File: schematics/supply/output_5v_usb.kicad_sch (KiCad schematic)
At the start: 79 parts, among them J2 USB_A, Q3 40N06, U10 LM2904, U11 IP2163, U12 LM2904, U13 TL432DBZ, U14 LM2904, U15 AMS1117-3.3, U2 EL817, U6 INA3221, U8 MC34063AD, U9 IRS2153S

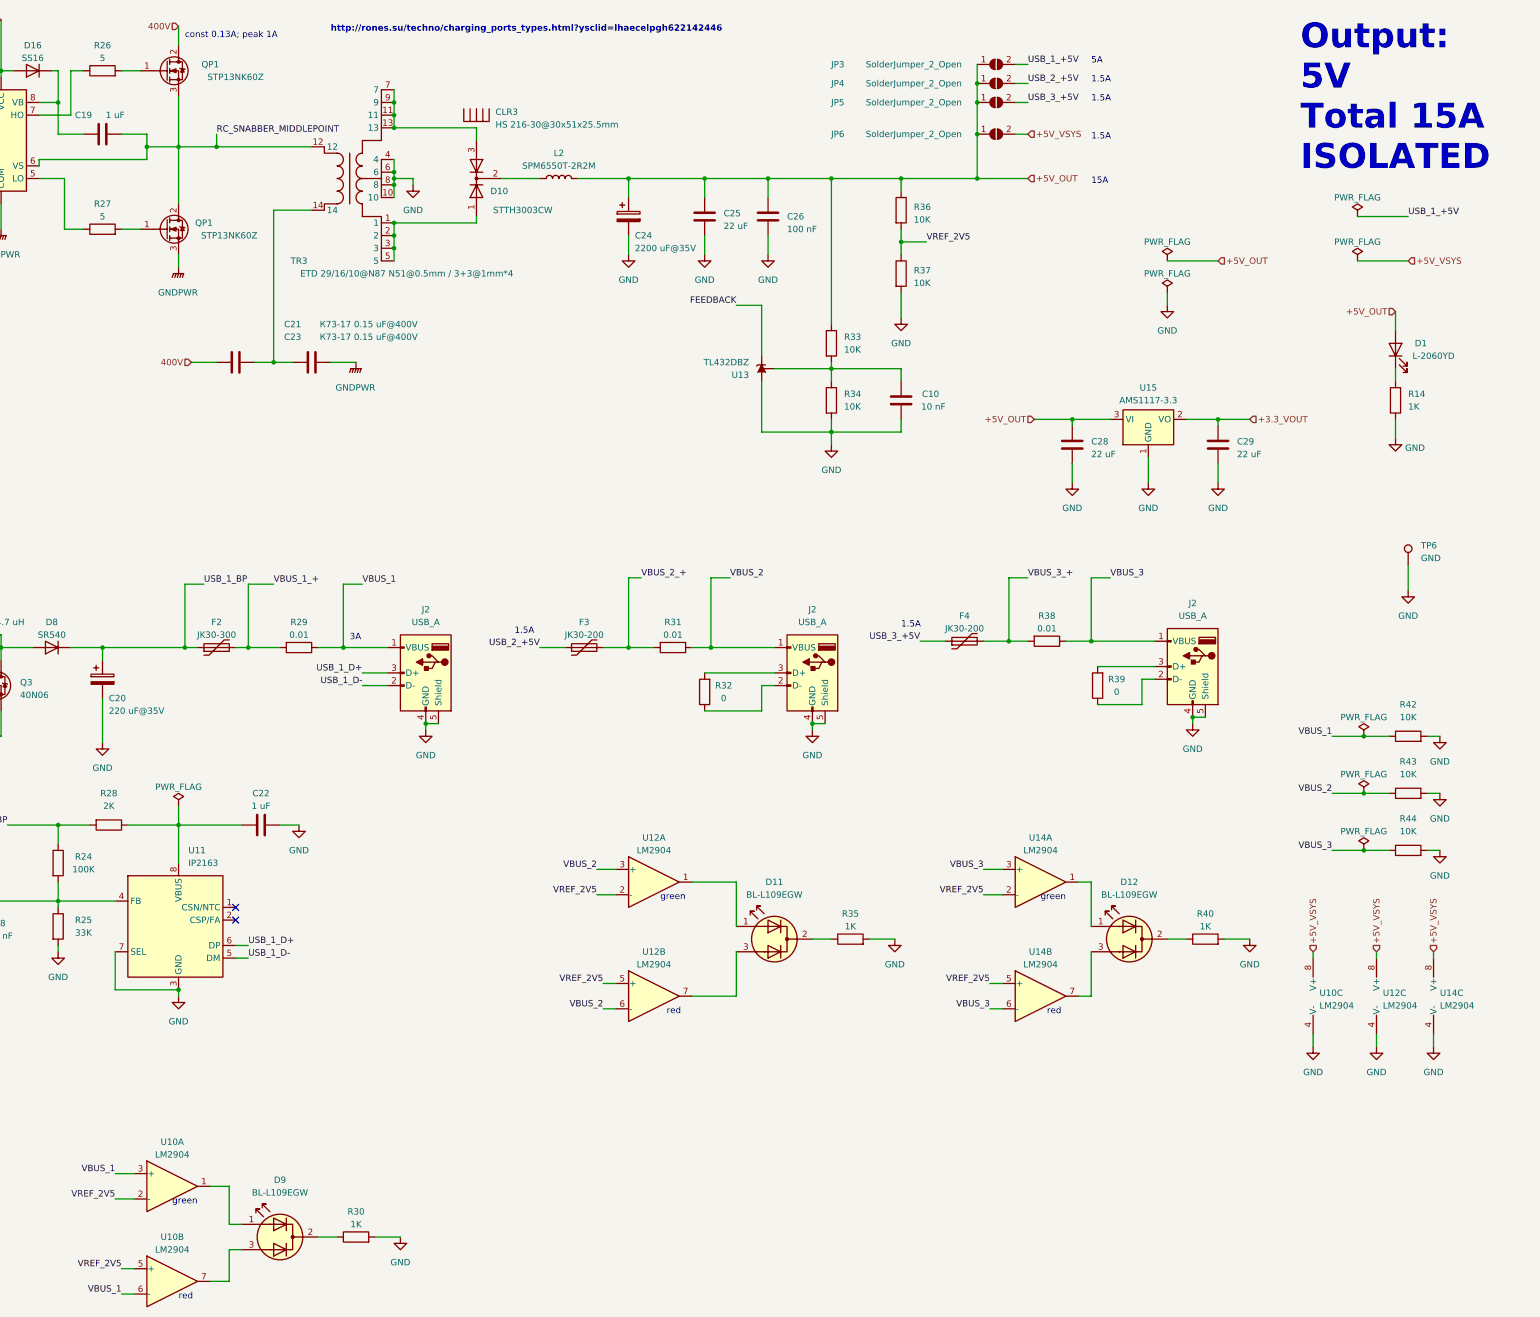
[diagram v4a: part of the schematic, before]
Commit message: prepare to add current measurement for a middle-current 5V and 3.3V lines
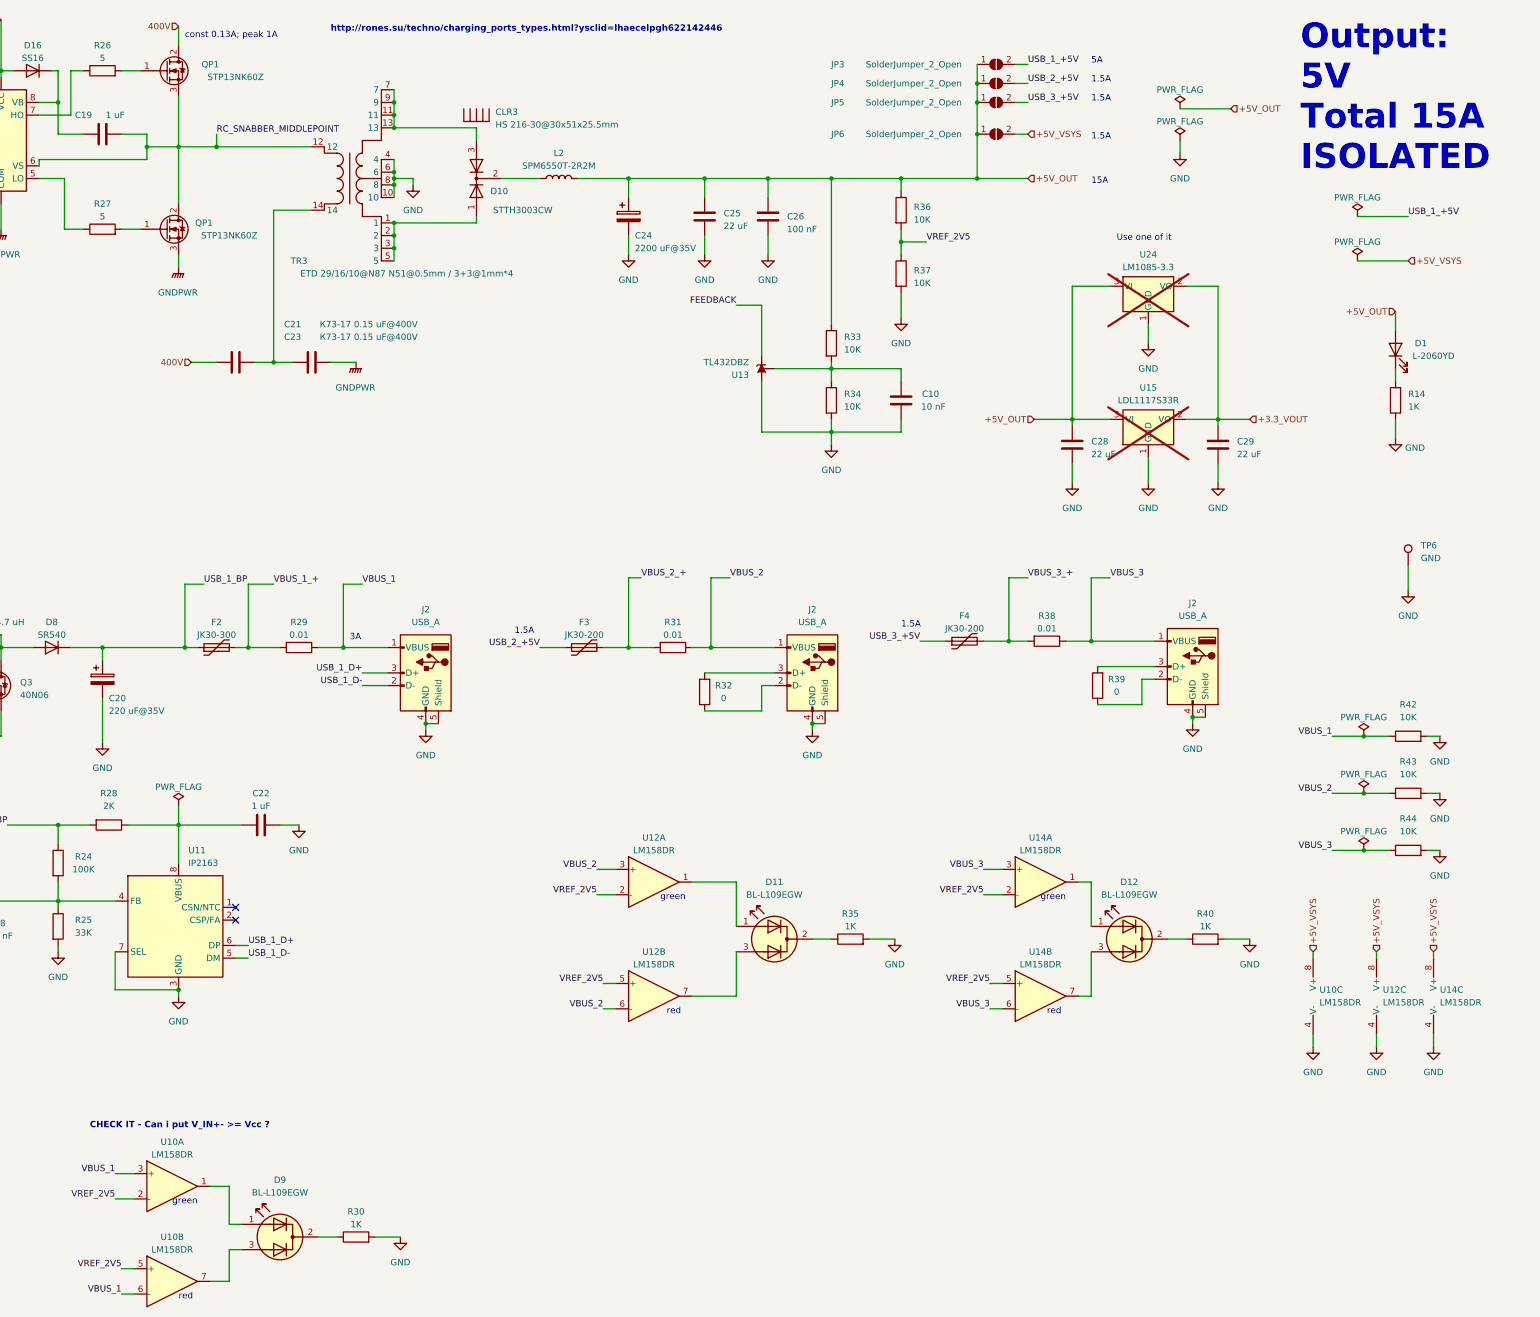
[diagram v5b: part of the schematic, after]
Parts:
- added U24: LM1085-3.3, Package_TO_SOT_SMD:TO-263-3_TabPin2, symbol Regulator_Linear:LM1085-3.3
- U10, U12, U14: value LM2904 -> LM158DR
- U15: value AMS1117-3.3 -> LDL1117S33R; now not fitted; now left out of the parts list
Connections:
- net +3.3_VOUT: now also U24.2 (VO)
- net +5V_OUT: now also U24.3 (VI)
- net GND: now also U24.1 (GND)
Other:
- note added: "CHECK IT - Can i put V_IN+- >= Vcc ?"
- note added: "Use one of it"
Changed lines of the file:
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@@
     (stroke (width 0) (type default))
   )
-  (wire (pts (xy 342.9 71.12) (xy 342.9 73.66))
+  (wire (pts (xy 345.44 40.64) (xy 345.44 43.18))
     (stroke (width 0) (type default))
   )
@@
     (stroke (width 0) (type default))
   )
+  (wire (pts (xy 323.85 69.85) (xy 323.85 96.52))
+    (stroke (width 0) (type default))
+  )
   (wire (pts (xy 149.86 129.54) (xy 146.05 129.54))
     (stroke (width 0) (type default))
@@
     (stroke (width 0) (type default))
   )
-  (wire (pts (xy 342.9 64.77) (xy 353.06 64.77))
+  (wire (pts (xy 345.44 34.29) (xy 355.6 34.29))
     (stroke (width 0) (type default))
   )
@@
     (stroke (width 0) (type default))
   )
+  (wire (pts (xy 331.47 69.85) (xy 323.85 69.85))
+    (stroke (width 0) (type default))
+  )
   (wire (pts (xy 29.21 139.7) (xy 31.75 139.7))
     (stroke (width 0) (type default))
   )
+  (wire (pts (xy 346.71 69.85) (xy 353.06 69.85))
+    (stroke (width 0) (type default))
+  )
   (wire (pts (xy 62.23 251.46) (xy 67.31 251.46))
     (stroke (width 0) (type default))
   )
+  (wire (pts (xy 353.06 69.85) (xy 353.06 96.52))
+    (stroke (width 0) (type default))
+  )
   (wire (pts (xy 327.66 140.97) (xy 340.36 140.97))
     (stroke (width 0) (type default))
@@
     (stroke (width 0) (type default))
   )
+  (wire (pts (xy 339.09 77.47) (xy 339.09 81.28))
+    (stroke (width 0) (type default))
+  )
   (wire (pts (xy 125.73 39.37) (xy 120.65 39.37))
     (stroke (width 0) (type default))
@@
     (effects (font (size 1.27 1.27)) (justify left bottom))
   )
+  (text "Use one of it" (at 332.74 60.96 0)
+    (effects (font (size 1.27 1.27)) (justify left bottom))
+  )
+  (text "CHECK IT - Can i put V_IN+- >= Vcc ?" (at 127 238.76 0)
+    (effects (font (size 1.27 1.27) (thickness 0.254) bold) (justify left bottom))
+  )
   (text "red" (at 318.77 215.9 0)
     (effects (font (size 1.27 1.27)) (justify left bottom))
@@
     (effects (font (size 1.27 1.27)) (justify left))
   )
-  (hierarchical_label "+5V_OUT" (shape input) (at 353.06 64.77 0) (fields_autoplaced)
+  (hierarchical_label "+5V_OUT" (shape input) (at 355.6 34.29 0) (fields_autoplaced)
     (effects (font (size 1.27 1.27)) (justify left))
   )
@@
   )
   (symbol (lib_id "Regulator_Linear:AMS1117-3.3") (at 339.09 96.52 0) (unit 1)
-    (in_bom yes) (on_board yes) (dnp no) (fields_autoplaced)
+    (in_bom no) (on_board yes) (dnp yes) (fields_autoplaced)
     (property "Reference" "U15" (at 339.09 90.17 0)
       (effects (font (size 1.27 1.27)))
     )
-    (property "Value" "AMS1117-3.3" (at 339.09 92.71 0)
+    (property "Value" "LDL1117S33R" (at 339.09 92.71 0)
       (effects (font (size 1.27 1.27)))
     )
@@
   (symbol (lib_id "Amplifier_Operational:LM2904") (at 374.65 212.09 0) (unit 3)
     (in_bom yes) (on_board yes) (dnp no) (fields_autoplaced)
-    (property "Reference" "U10" (at 373.38 211.455 0)
+    (property "Reference" "U10" (at 373.38 210.82 0)
       (effects (font (size 1.27 1.27)) (justify left))
     )
-    (property "Value" "LM2904" (at 373.38 213.995 0)
+    (property "Value" "LM158DR" (at 373.38 213.36 0)
       (effects (font (size 1.27 1.27)) (justify left))
     )
@@
       (effects (font (size 1.27 1.27)))
     )
-    (property "Value" "LM2904" (at 143.51 243.84 0)
+    (property "Value" "LM158DR" (at 143.51 243.84 0)
       (effects (font (size 1.27 1.27)))
     )
@@
       (effects (font (size 1.27 1.27)))
     )
-    (property "Value" "LM2904" (at 317.5 205.74 0)
+    (property "Value" "LM158DR" (at 317.5 205.74 0)
       (effects (font (size 1.27 1.27)))
     )
@@
       (effects (font (size 1.27 1.27)))
     )
-    (property "Value" "LM2904" (at 317.5 182.88 0)
+    (property "Value" "LM158DR" (at 317.5 182.88 0)
       (effects (font (size 1.27 1.27)))
     )
@@
     )
   )
-  (symbol (lib_id "power:PWR_FLAG") (at 342.9 71.12 0) (unit 1)
+  (symbol (lib_id "power:PWR_FLAG") (at 345.44 40.64 0) (unit 1)
     (in_bom yes) (on_board yes) (dnp no) (fields_autoplaced)
-    (property "Reference" "#FLG011" (at 342.9 69.215 0)
+    (property "Reference" "#FLG011" (at 345.44 38.735 0)
       (effects (font (size 1.27 1.27)) hide)
     )
-    (property "Value" "PWR_FLAG" (at 342.9 67.31 0)
+    (property "Value" "PWR_FLAG" (at 345.44 36.83 0)
       (effects (font (size 1.27 1.27)))
     )
-    (property "Footprint" "" (at 342.9 71.12 0)
+    (property "Footprint" "" (at 345.44 40.64 0)
       (effects (font (size 1.27 1.27)) hide)
     )
-    (property "Datasheet" "~" (at 342.9 71.12 0)
+    (property "Datasheet" "~" (at 345.44 40.64 0)
       (effects (font (size 1.27 1.27)) hide)
     )
@@
     )
   )
-  (symbol (lib_id "power:PWR_FLAG") (at 342.9 64.77 0) (unit 1)
+  (symbol (lib_id "power:PWR_FLAG") (at 345.44 34.29 0) (unit 1)
     (in_bom yes) (on_board yes) (dnp no) (fields_autoplaced)
-    (property "Reference" "#FLG010" (at 342.9 62.865 0)
+    (property "Reference" "#FLG010" (at 345.44 32.385 0)
       (effects (font (size 1.27 1.27)) hide)
     )
-    (property "Value" "PWR_FLAG" (at 342.9 60.96 0)
+    (property "Value" "PWR_FLAG" (at 345.44 30.48 0)
       (effects (font (size 1.27 1.27)))
     )
-    (property "Footprint" "" (at 342.9 64.77 0)
+    (property "Footprint" "" (at 345.44 34.29 0)
       (effects (font (size 1.27 1.27)) hide)
     )
-    (property "Datasheet" "~" (at 342.9 64.77 0)
+    (property "Datasheet" "~" (at 345.44 34.29 0)
       (effects (font (size 1.27 1.27)) hide)
     )
@@
   (symbol (lib_id "Amplifier_Operational:LM2904") (at 387.35 212.09 0) (unit 3)
     (in_bom yes) (on_board yes) (dnp no) (fields_autoplaced)
-    (property "Reference" "U12" (at 386.08 211.455 0)
+    (property "Reference" "U12" (at 386.08 210.82 0)
       (effects (font (size 1.27 1.27)) (justify left))
     )
-    (property "Value" "LM2904" (at 386.08 213.995 0)
+    (property "Value" "LM158DR" (at 386.08 213.36 0)
       (effects (font (size 1.27 1.27)) (justify left))
     )
@@
       (effects (font (size 1.27 1.27)))
     )
-    (property "Value" "LM2904" (at 143.51 262.89 0)
+    (property "Value" "LM158DR" (at 143.51 262.89 0)
       (effects (font (size 1.27 1.27)))
     )
@@
     )
   )
+  (symbol (lib_id "power:GND") (at 339.09 81.28 0) (unit 1)
+    (in_bom yes) (on_board yes) (dnp no) (fields_autoplaced)
+    (property "Reference" "#PWR0100" (at 339.09 87.63 0)
+      (effects (font (size 1.27 1.27)) hide)
+    )
+    (property "Value" "GND" (at 339.09 86.36 0)
+      (effects (font (size 1.27 1.27)))
+    )
+    (property "Footprint" "" (at 339.09 81.28 0)
+      (effects (font (size 1.27 1.27)) hide)
+    )
+    (property "Datasheet" "" (at 339.09 81.28 0)
+      (effects (font (size 1.27 1.27)) hide)
+    )
+    (pin "1")
+    (instances
+      (project "supply"
+        (path "/1e139717-fcd1-4008-a6ea-4c993845e928/bcabd54f-a555-4409-9a4f-89c20a3d7682"
+          (reference "#PWR0100") (unit 1)
+        )
+      )
+    )
+  )
   (symbol (lib_id "Device:R") (at 130.81 177.8 270) (unit 1)
     (in_bom yes) (on_board yes) (dnp no)
@@
     )
   )
+  (symbol (lib_id "Regulator_Linear:LM1085-3.3") (at 339.09 69.85 0) (unit 1)
+    (in_bom no) (on_board yes) (dnp yes) (fields_autoplaced)
+    (property "Reference" "U24" (at 339.09 63.5 0)
+      (effects (font (size 1.27 1.27)))
+    )
+    (property "Value" "LM1085-3.3" (at 339.09 66.04 0)
+      (effects (font (size 1.27 1.27)))
+    )
+    (property "Footprint" "Package_TO_SOT_SMD:TO-263-3_TabPin2" (at 339.09 63.5 0)
+      (effects (font (size 1.27 1.27) italic) hide)
+    )
+    (property "Datasheet" "http://www.ti.com/lit/ds/symlink/lm1085.pdf" (at 339.09 69.85 0)
+      (effects (font (size 1.27 1.27)) hide)
+    )
+    (pin "1")
+    (pin "2")
+    (pin "3")
+    (instances
+      (project "supply"
+        (path "/1e139717-fcd1-4008-a6ea-4c993845e928/bcabd54f-a555-4409-9a4f-89c20a3d7682"
+          (reference "U24") (unit 1)
+        )
+      )
+    )
+  )
   (symbol (lib_id "Amplifier_Operational:LM2904") (at 398.78 212.09 0) (unit 3)
     (in_bom yes) (on_board yes) (dnp no) (fields_autoplaced)
-    (property "Reference" "U14" (at 397.51 211.455 0)
+    (property "Reference" "U14" (at 397.51 210.82 0)
       (effects (font (size 1.27 1.27)) (justify left))
     )
-    (property "Value" "LM2904" (at 397.51 213.995 0)
+    (property "Value" "LM158DR" (at 397.51 213.36 0)
       (effects (font (size 1.27 1.27)) (justify left))
     )
@@
     )
   )
-  (symbol (lib_id "power:GND") (at 342.9 73.66 0) (unit 1)
+  (symbol (lib_id "power:GND") (at 345.44 43.18 0) (unit 1)
     (in_bom yes) (on_board yes) (dnp no) (fields_autoplaced)
-    (property "Reference" "#PWR030" (at 342.9 80.01 0)
+    (property "Reference" "#PWR030" (at 345.44 49.53 0)
       (effects (font (size 1.27 1.27)) hide)
     )
-    (property "Value" "GND" (at 342.9 78.74 0)
+    (property "Value" "GND" (at 345.44 48.26 0)
       (effects (font (size 1.27 1.27)))
     )
-    (property "Footprint" "" (at 342.9 73.66 0)
+    (property "Footprint" "" (at 345.44 43.18 0)
       (effects (font (size 1.27 1.27)) hide)
     )
-    (property "Datasheet" "" (at 342.9 73.66 0)
+    (property "Datasheet" "" (at 345.44 43.18 0)
       (effects (font (size 1.27 1.27)) hide)
     )
@@
       (effects (font (size 1.27 1.27)))
     )
-    (property "Value" "LM2904" (at 240.03 205.74 0)
+    (property "Value" "LM158DR" (at 240.03 205.74 0)
       (effects (font (size 1.27 1.27)))
     )
@@
       (effects (font (size 1.27 1.27)))
     )
-    (property "Value" "LM2904" (at 240.03 182.88 0)
+    (property "Value" "LM158DR" (at 240.03 182.88 0)
       (effects (font (size 1.27 1.27)))
     )

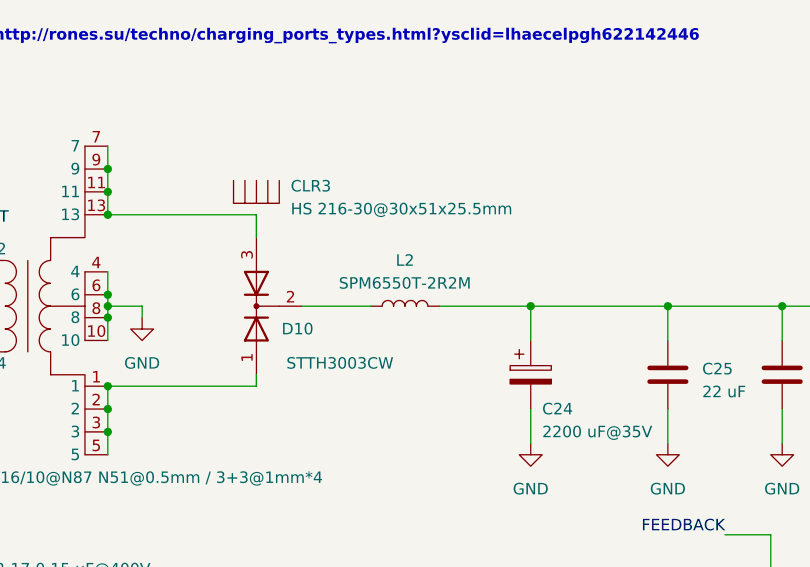
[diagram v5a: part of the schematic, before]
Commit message: prepare to replace inductor on 5V power line
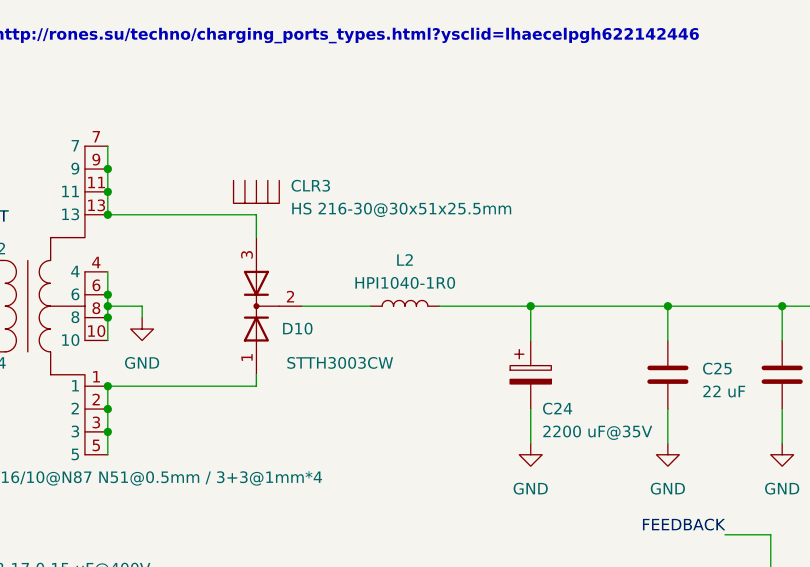
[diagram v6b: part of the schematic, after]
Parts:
- L2: value SPM6550T-2R2M -> HPI1040-1R0; footprint Inductor_SMD:L_Sumida_CDMC6D28_7.25x6.5mm -> Library:Ferrocore-HPI1040
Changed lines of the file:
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@@
       (effects (font (size 1.27 1.27)))
     )
-    (property "Value" "SPM6550T-2R2M" (at 220.98 45.72 90)
+    (property "Value" "HPI1040-1R0" (at 220.98 45.72 90)
       (effects (font (size 1.27 1.27)))
     )
-    (property "Footprint" "Inductor_SMD:L_Sumida_CDMC6D28_7.25x6.5mm" (at 220.98 48.26 0)
+    (property "Footprint" "Library:Ferrocore-HPI1040" (at 220.98 48.26 0)
       (effects (font (size 1.27 1.27)) hide)
     )
